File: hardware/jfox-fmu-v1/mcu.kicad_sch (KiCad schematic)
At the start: 1 part, among them U10 STM32H753IIT6

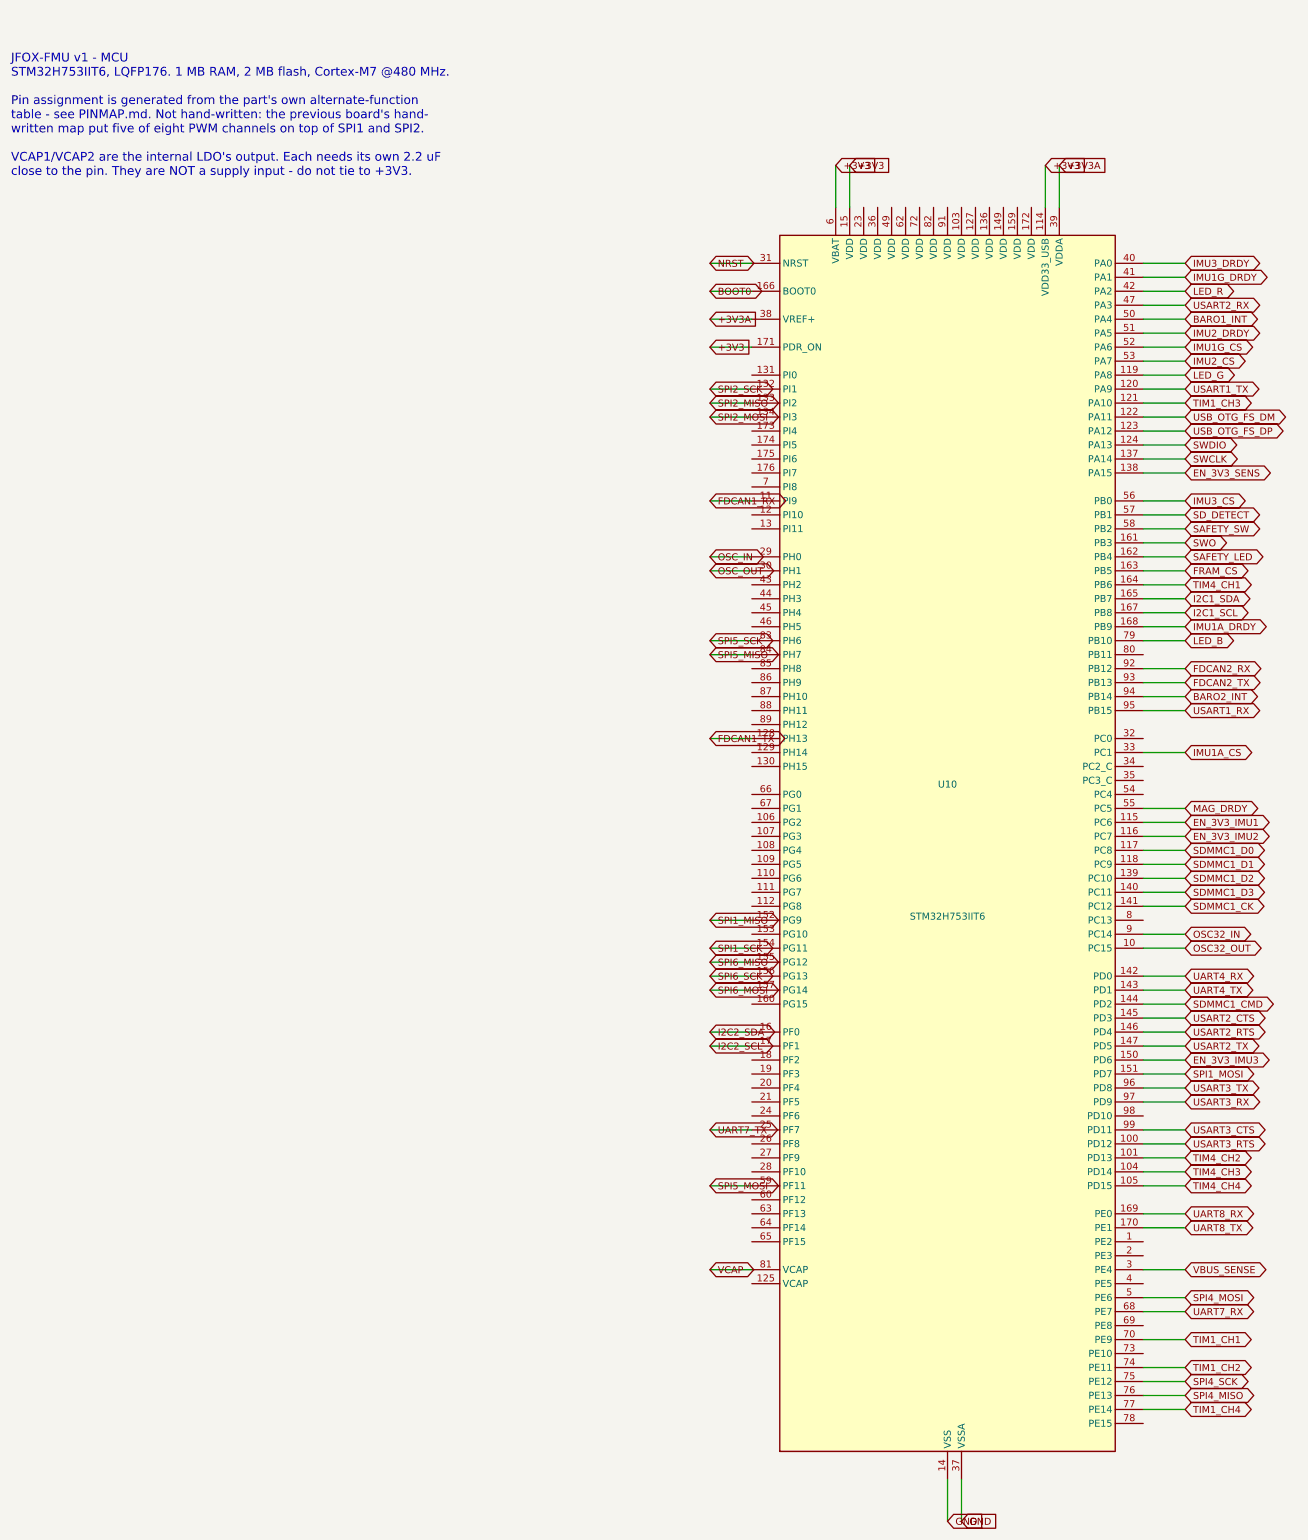
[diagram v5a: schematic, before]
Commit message: A4 title-blocked sheets, and the 25 power pins that were never wired
Every sheet now carries a title block naming JFOX Aircraft Co., Ltd., with a
per-sheet title, revision, date and the notes that used to float as loose text.

A4 PORTRAIT, not landscape, and not by preference. The STM32H753IITx symbol is
a single unit - KiCad's library gives it only _0_1 body and _1_1 pin
sub-symbols, so it cannot be split across pages - and its 176 pins span
231.1 mm. A4 landscape offers about 180 mm of usable height and would cut the
MCU in half. Portrait offers 237 mm. The part fits with 2 mm to spare, which
is why the page margin is 2 mm: it is the largest margin that still holds an
LQFP176, not a number chosen for looks.

The frame geometry was measured, not assumed - an empty A4 portrait sheet
plotted through kicad-cli, frame read off the SVG at 12,12 -> 198,285 with the
title block claiming x >= 90, y >= 253.

Three defects the work surfaced, in rising order of how much they mattered:

Every sheet had content at negative coordinates, off the page entirely, where
KiCad edits it happily and the plotter crops it away. Nothing had complained
because nothing was looking. fit() now translates each sheet into the drawable
area and refuses - loudly - to emit one that does not fit, because a schematic
that is silently cropped lies about the board.

fit() then passed the power sheet while its rightmost label sat 8.6 mm past
the frame. A global label's angle is the direction its CONNECTION faces, so
the text runs the opposite way; reading it the intuitive way put every
estimated extent on the wrong side of its anchor. That is worse than not
estimating: it reports "inside the frame" precisely when labels hang off it.
Caught by measuring KiCad's own plotted geometry instead of trusting the
estimate - which is what check_fmu_sheets.py now does on every sheet, with
--exclude-drawing-sheet so only the circuit is measured.

And centring the sheets by (SAFE_W - w) / 2 shifted every wire off th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
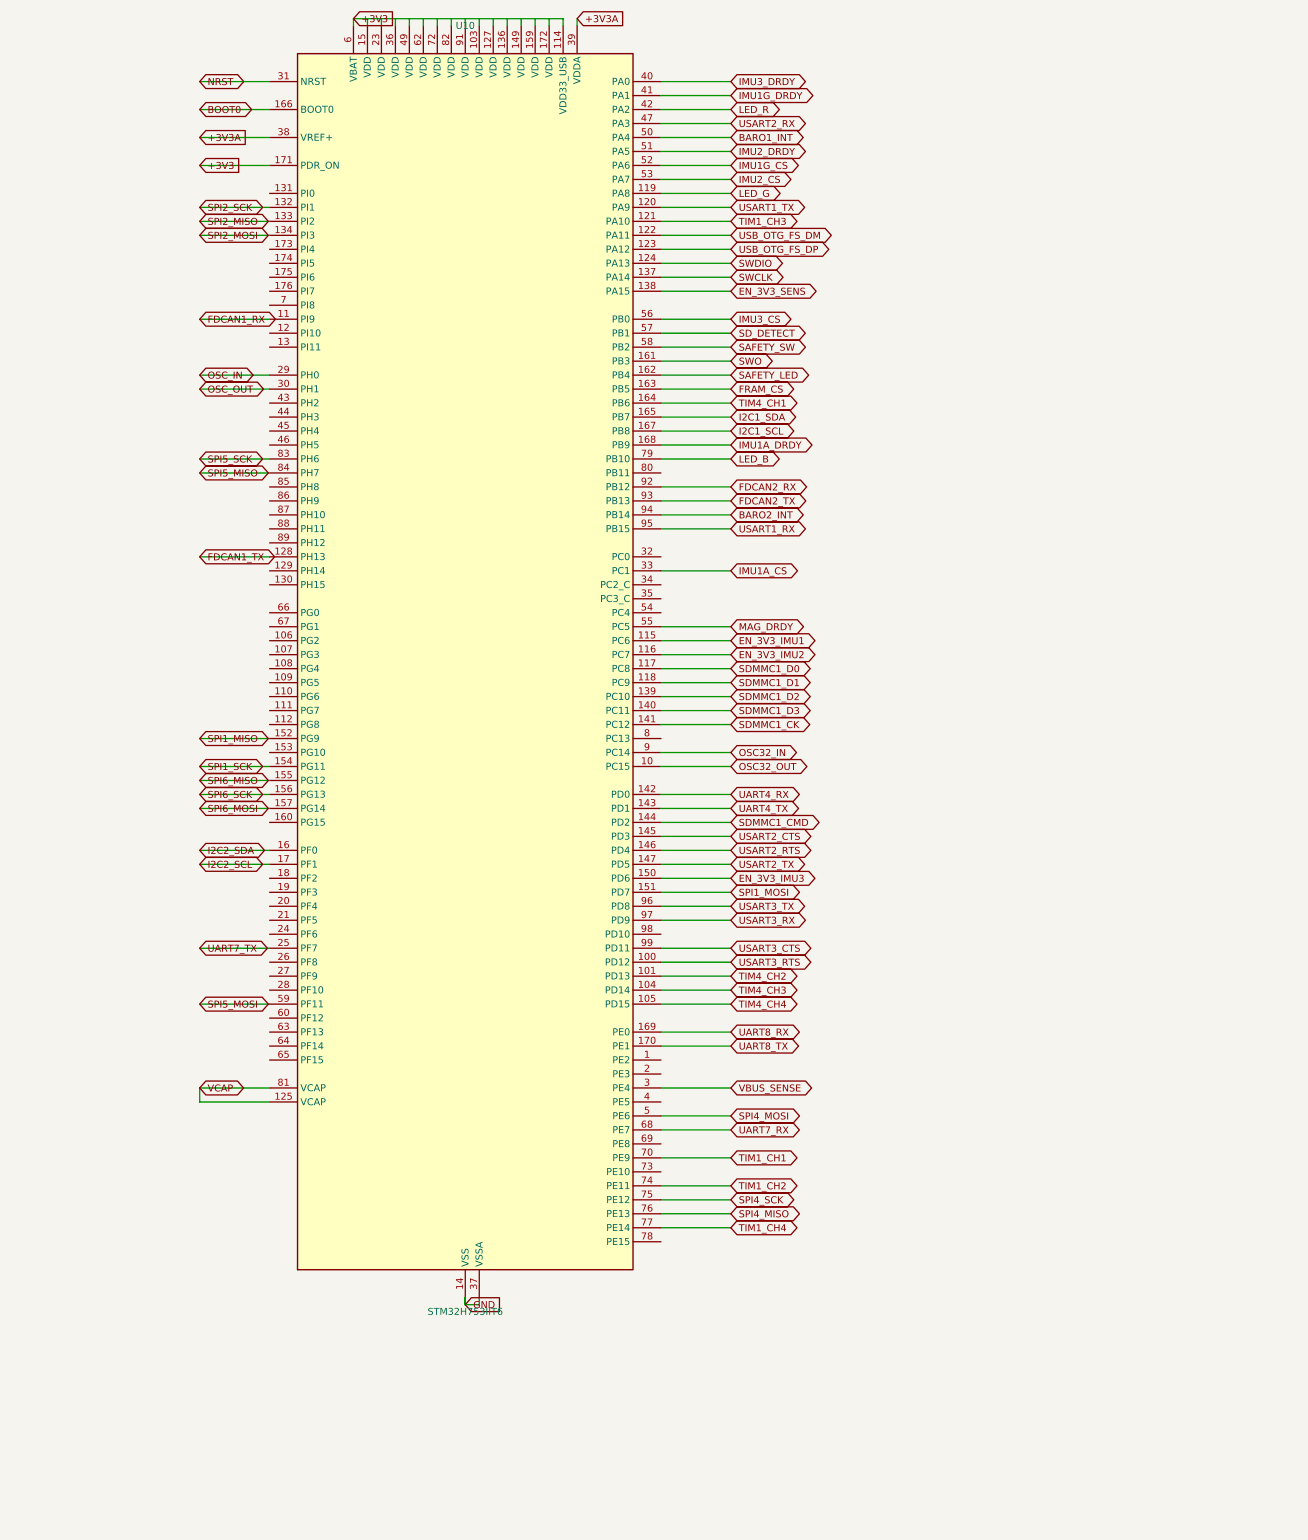
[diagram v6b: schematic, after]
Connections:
- net +3V3: no longer U10.15 (VDD)
- net VCAP: now also U10.125 (VCAP)
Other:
- note removed: "JFOX-FMU v1 - MCU STM32H753IIT6, LQFP176. 1 MB RAM, 2 MB flash, Cortex-M7 @480 MHz. Pin assignment is generated from the part's own alternate-function table - see PINMAP.md. Not hand-written: the previous board's hand- written map put five of eight PWM channels on top of SPI1 and SPI2. VCAP1/VCAP2 are the internal LDO's output. Each needs its own 2.2 uF close to the pin. They are NOT a supply inp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"
- company: (none) -> JFOX Aircraft Co., Ltd.
- title: (none) -> MCU

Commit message: Footprint every part, and verify each one exists
58 of 58 components now carry a footprint chosen against the package its
datasheet specifies, and check_fmu_footprints.py confirms every name resolves
to a file on disk.

Three of the names this design was carrying did not. The symbol library named
`Sensor_Motion:InvenSense_QFN-14_3x3mm_P0.5mm` and
`Sensor_Pressure:Bosch_LGA-10_2x2mm_P0.35mm`, neither of which is a footprint
in any installed library - both plausible, both fiction. The third was worse:
`Package_LGA:Bosch_LGA-14_3x2.5mm_P0.5mm` is real, matches the InvenSense
package on every word of its name, and is drawn for the BMI160 with 0.675 mm
pads where InvenSense wants 0.475 mm.

Notable choices, each traceable:
  LTC4417CGN  GN is the 16-lead narrow SSOP.
  TPS62132    RGT 3x3 VQFN. TI's land drawing (4222419/E) gives the exposed
              pad as 1.55 mm; KiCad's 1.6 mm variant is closest. Thermal-via
              variant, since the datasheet is explicit that the pad must be
              soldered and that dissipation limits output power.
  Bulk caps   4u7/10u/22u get an 0805, not the 0402 every other capacitor
              gets. Assigning one size to all of them produces a board that
              cannot be built from the BOM it ships with.
  L1          a generic 1210 land, and labelled as such - the 2.2 uH part is
              not chosen yet, since saturation current and DCR still have to
              be picked against the real 550 mA peak.

The checker was wrong on its first run, in a way worth recording because the
failure mode is self-concealing. It matched ref, value and footprint in one
regex with the footprint group optional, so a component with no footprint -
precisely what it exists to find - failed to match at all, dropped out of the
list, and the run reported "every component maps to a footprint" while the
count quietly fell by one. A check whose failure mode is to stop seeing the
failure is worse than no check. Now it splits into per-com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
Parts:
- U10: footprint (none) -> Package_QFP:LQFP-176_24x24mm_P0.5mm
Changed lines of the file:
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@@
+		)
+		)
+		(property "Footprint" "Package_QFP:LQFP-176_24x24mm_P0.5mm"
+			(at 102.87 132.08 0)
+			(hide yes)
+			(effects
+			(font
+				(size 1.27 1.27)
+			)
 		)
 		)
 		(instances
 			(project "jfox-fmu"
-				(path "/755ae06a-7c62-4250-9a10-6b0d9e1950ba"
+				(path "/5e1b880c-8a1f-45c2-8c63-05aec060b2ed"
 					(reference "U10")
 					(unit 1)
